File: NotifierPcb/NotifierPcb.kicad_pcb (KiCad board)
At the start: 2 copper layers, 81.6 x 97.9 mm, 30 parts, among them IC1 CD4067BEE4, IC2 ESP32-WROOM-32E__8MB_, J1 RC_433_MHZ_RF, J2 UART_Conn, J3 Power_Conn, J5 Vcc, J6 Vcc, U1 HT75xx-1-SOT89

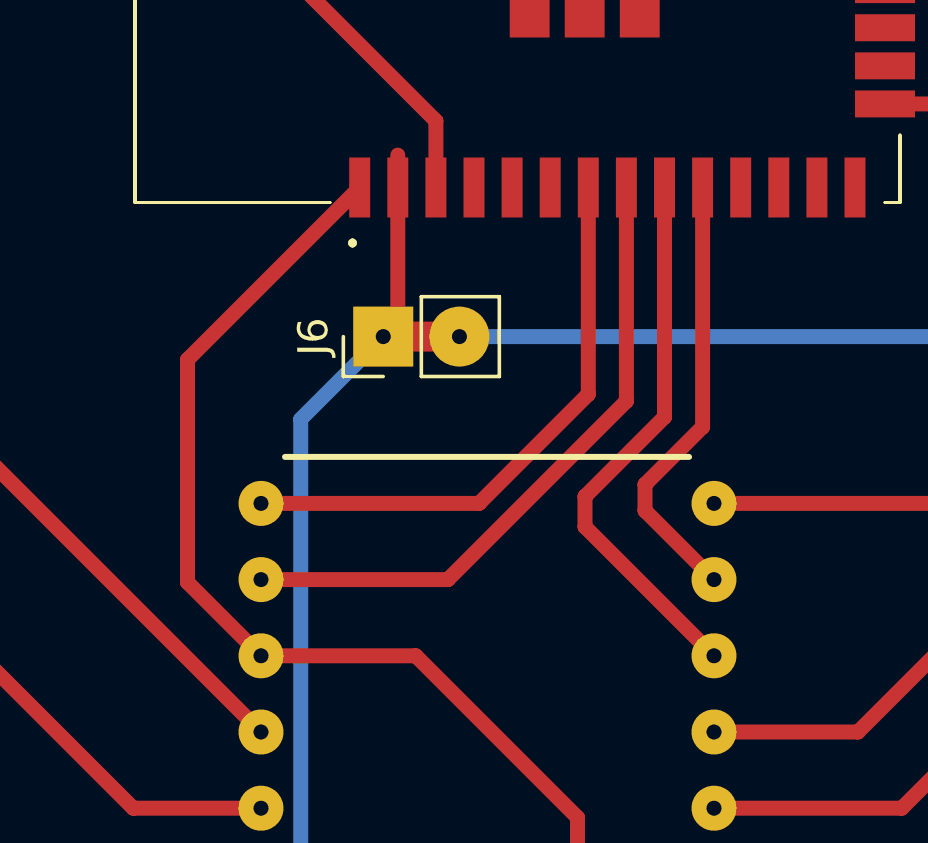
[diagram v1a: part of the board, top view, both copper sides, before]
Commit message: FIX: using only-input pin
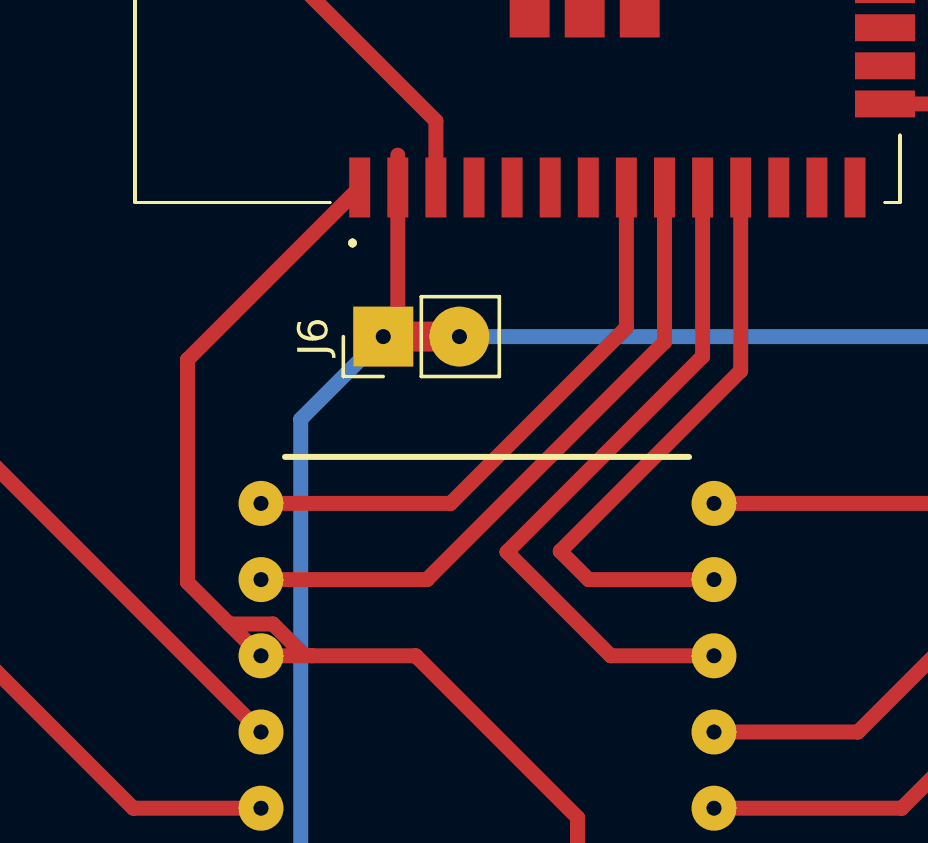
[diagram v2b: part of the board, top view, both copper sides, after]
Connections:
- IC2 pad 10: BIT1 -> BIT0
- IC2 pad 11: unconnected-(IC2-Pad11) -> BIT1
- IC2 pad 7: BIT3 -> unconnected-(IC2-Pad7)
- IC2 pad 8: BIT2 -> BIT3
- IC2 pad 9: BIT0 -> BIT2
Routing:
- net BIT1: track 14.8 -> 20.1 mm
- net BIT0: track 18.5 -> 23.2 mm
- net GND: track 197.6 -> 200.5 mm
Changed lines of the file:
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@@
   (net 25 "unconnected-(IC2-Pad5)")
   (net 26 "unconnected-(IC2-Pad6)")
-  (net 27 "unconnected-(IC2-Pad11)")
+  (net 27 "unconnected-(IC2-Pad7)")
   (net 28 "unconnected-(IC2-Pad12)")
   (net 29 "unconnected-(IC2-Pad13)")
@@
       (net 26 "unconnected-(IC2-Pad6)") (pinfunction "IO34") (pintype "passive"))
     (pad "7" smd rect (at -8.5 2.36 180) (size 0.7 2) (layers "F.Cu" "F.Paste" "F.Mask")
-      (net 13 "BIT3") (pinfunction "IO35") (pintype "passive"))
+      (net 27 "unconnected-(IC2-Pad7)") (pinfunction "IO35") (pintype "passive"))
     (pad "8" smd rect (at -8.5 3.63 180) (size 0.7 2) (layers "F.Cu" "F.Paste" "F.Mask")
-      (net 14 "BIT2") (pinfunction "IO32") (pintype "passive"))
+      (net 13 "BIT3") (pinfunction "IO32") (pintype "passive"))
     (pad "9" smd rect (at -8.5 4.9 180) (size 0.7 2) (layers "F.Cu" "F.Paste" "F.Mask")
-      (net 10 "BIT0") (pinfunction "IO33") (pintype "passive"))
+      (net 14 "BIT2") (pinfunction "IO33") (pintype "passive"))
     (pad "10" smd rect (at -8.5 6.17 180) (size 0.7 2) (layers "F.Cu" "F.Paste" "F.Mask")
-      (net 11 "BIT1") (pinfunction "IO25") (pintype "passive"))
+      (net 10 "BIT0") (pinfunction "IO25") (pintype "passive"))
     (pad "11" smd rect (at -8.5 7.44 180) (size 0.7 2) (layers "F.Cu" "F.Paste" "F.Mask")
-      (net 27 "unconnected-(IC2-Pad11)") (pinfunction "IO26") (pintype "passive"))
+      (net 11 "BIT1") (pinfunction "IO26") (pintype "passive"))
     (pad "12" smd rect (at -8.5 8.71 180) (size 0.7 2) (layers "F.Cu" "F.Paste" "F.Mask")
       (net 28 "unconnected-(IC2-Pad12)") (pinfunction "IO27") (pintype "passive"))
@@
   (segment (start 168.85 74.15) (end 168.9 74.15) (width 1) (layer "F.Cu") (net 9))
   (segment (start 147.55 90.65) (end 152.35 90.65) (width 0.5) (layer "F.Cu") (net 9))
-  (segment (start 145.9 80.15) (end 143.25 82.8) (width 0.5) (layer "F.Cu") (net 10))
-  (segment (start 145.9 72.5) (end 145.9 80.15) (width 0.5) (layer "F.Cu") (net 10))
-  (segment (start 143.25 83.81) (end 147.55 88.11) (width 0.5) (layer "F.Cu") (net 10))
-  (segment (start 143.25 82.8) (end 143.25 83.81) (width 0.5) (layer "F.Cu") (net 10))
-  (segment (start 147.17 80.48) (end 145.25 82.4) (width 0.5) (layer "F.Cu") (net 11))
-  (segment (start 147.17 72.5) (end 147.17 80.48) (width 0.5) (layer "F.Cu") (net 11))
-  (segment (start 145.25 83.27) (end 147.55 85.57) (width 0.5) (layer "F.Cu") (net 11))
-  (segment (start 145.25 82.4) (end 145.25 83.27) (width 0.5) (layer "F.Cu") (net 11))
+  (segment (start 140.65 84.65) (end 144.11 88.11) (width 0.5) (layer "F.Cu") (net 10))
+  (segment (start 147.17 78.13) (end 140.65 84.65) (width 0.5) (layer "F.Cu") (net 10))
+  (segment (start 147.17 72.5) (end 147.17 78.13) (width 0.5) (layer "F.Cu") (net 10))
+  (segment (start 144.11 88.11) (end 147.55 88.11) (width 0.5) (layer "F.Cu") (net 10))
+  (segment (start 148.44 72.5) (end 148.44 78.61) (width 0.5) (layer "F.Cu") (net 11))
+  (segment (start 148.44 78.61) (end 142.425 84.625) (width 0.5) (layer "F.Cu") (net 11))
+  (segment (start 143.37 85.57) (end 147.55 85.57) (width 0.5) (layer "F.Cu") (net 11))
+  (segment (start 142.425 84.625) (end 143.37 85.57) (width 0.5) (layer "F.Cu") (net 11))
   (segment (start 111.55 58.672349) (end 111.55 63.535) (width 0.5) (layer "F.Cu") (net 12))
   (segment (start 144.75 118.6) (end 144.75 122.05) (width 0.5) (layer "F.Cu") (net 12))
@@
   (segment (start 143.0665 116.9165) (end 144.75 118.6) (width 0.5) (layer "F.Cu") (net 12))
   (segment (start 155.72 83.03) (end 147.55 83.03) (width 0.5) (layer "F.Cu") (net 12))
-  (segment (start 132.45 88.11) (end 137.61 88.11) (width 0.5) (layer "F.Cu") (net 12))
   (segment (start 156.115 69.715) (end 158.05 71.65) (width 0.5) (layer "F.Cu") (net 12))
   (segment (start 103.775 57.275) (end 110.152651 57.275) (width 0.5) (layer "F.Cu") (net 12))
@@
   (segment (start 128.46 48.22) (end 135.74 55.5) (width 0.5) (layer "F.Cu") (net 12))
   (segment (start 118.007651 58.672349) (end 128.46 48.22) (width 0.5) (layer "F.Cu") (net 12))
+  (segment (start 130 85.66) (end 131.17 86.83) (width 0.5) (layer "F.Cu") (net 12))
   (segment (start 177 67.5) (end 174.75 69.75) (width 0.5) (layer "F.Cu") (net 12))
   (segment (start 167.81 67.71) (end 167.81 61.3) (width 0.5) (layer "F.Cu") (net 12))
   (segment (start 110.152651 57.275) (end 111.55 58.672349) (width 0.5) (layer "F.Cu") (net 12))
   (segment (start 173.9 49.35) (end 173.9 52.35) (width 0.5) (layer "F.Cu") (net 12))
+  (segment (start 132.45 88.11) (end 134.14 88.11) (width 0.5) (layer "F.Cu") (net 12))
   (segment (start 130 78.24) (end 130 85.66) (width 0.5) (layer "F.Cu") (net 12))
   (segment (start 174.75 69.75) (end 169.85 69.75) (width 0.5) (layer "F.Cu") (net 12))
@@
   (segment (start 143.0665 123.7335) (end 142.85 123.95) (width 1) (layer "F.Cu") (net 12))
   (segment (start 153.25 69.715) (end 156.115 69.715) (width 0.5) (layer "F.Cu") (net 12))
+  (segment (start 134.14 88.11) (end 137.61 88.11) (width 0.5) (layer "F.Cu") (net 12))
+  (segment (start 132.85 87.05) (end 133.91 88.11) (width 0.5) (layer "F.Cu") (net 12))
+  (segment (start 131.17 86.83) (end 132.45 88.11) (width 0.5) (layer "F.Cu") (net 12))
   (segment (start 137.61 88.11) (end 143 93.5) (width 0.5) (layer "F.Cu") (net 12))
   (segment (start 111.55 58.672349) (end 118.007651 58.672349) (width 0.5) (layer "F.Cu") (net 12))
@@
   (segment (start 143 93.5) (end 143 116.85) (width 0.5) (layer "F.Cu") (net 12))
   (segment (start 169.85 69.75) (end 167.81 67.71) (width 0.5) (layer "F.Cu") (net 12))
-  (segment (start 130 85.66) (end 132.45 88.11) (width 0.5) (layer "F.Cu") (net 12))
-  (segment (start 139.72 83.03) (end 132.45 83.03) (width 0.5) (layer "F.Cu") (net 13))
-  (segment (start 143.36 72.5) (end 143.36 79.39) (width 0.5) (layer "F.Cu") (net 13))
-  (segment (start 143.36 79.39) (end 139.72 83.03) (width 0.5) (layer "F.Cu") (net 13))
-  (segment (start 138.68 85.57) (end 132.45 85.57) (width 0.5) (layer "F.Cu") (net 14))
-  (segment (start 144.63 79.62) (end 138.68 85.57) (width 0.5) (layer "F.Cu") (net 14))
-  (segment (start 144.63 72.5) (end 144.63 79.62) (width 0.5) (layer "F.Cu") (net 14))
+  (segment (start 131.39 87.05) (end 132.85 87.05) (width 0.5) (layer "F.Cu") (net 12))
+  (segment (start 132.45 83.03) (end 138.77 83.03) (width 0.5) (layer "F.Cu") (net 13))
+  (segment (start 144.63 77.17) (end 144.63 72.5) (width 0.5) (layer "F.Cu") (net 13))
+  (segment (start 138.77 83.03) (end 144.63 77.17) (width 0.5) (layer "F.Cu") (net 13))
+  (segment (start 145.9 77.65) (end 145.9 72.5) (width 0.5) (layer "F.Cu") (net 14))
+  (segment (start 137.98 85.57) (end 145.9 77.65) (width 0.5) (layer "F.Cu") (net 14))
+  (segment (start 132.45 85.57) (end 137.98 85.57) (width 0.5) (layer "F.Cu") (net 14))
   (segment (start 114.65 73.1) (end 114.9 73.1) (width 1) (layer "F.Cu") (net 15))
   (segment (start 114.9 73.1) (end 132.45 90.65) (width 0.5) (layer "F.Cu") (net 15))

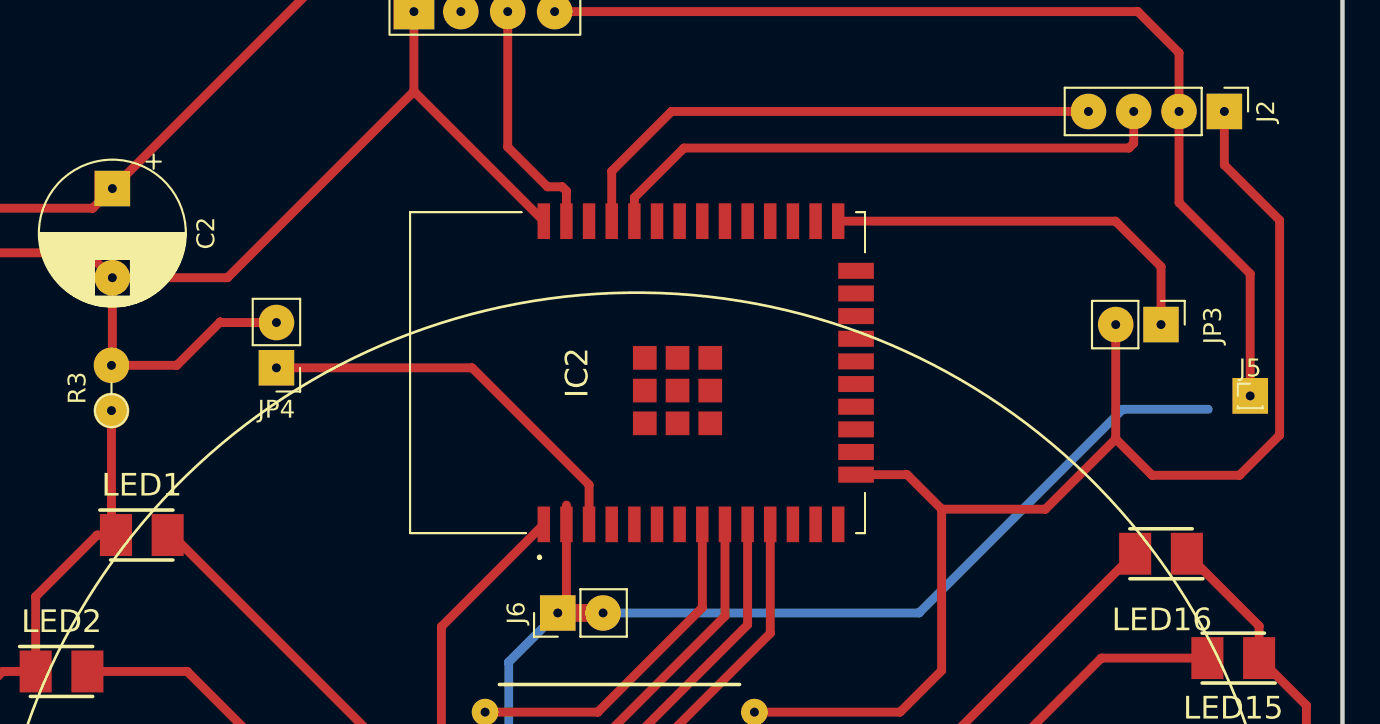
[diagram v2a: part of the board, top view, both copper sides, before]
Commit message: add pullup resistor for strapping pins
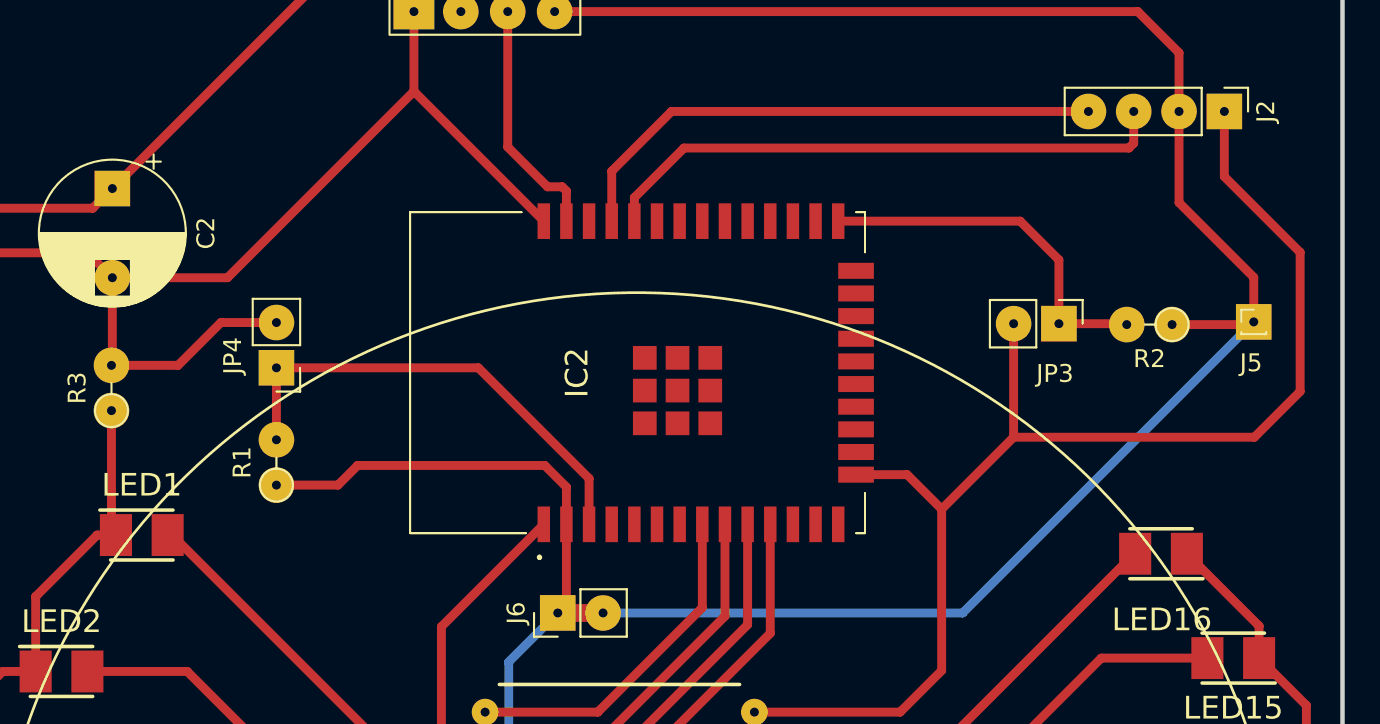
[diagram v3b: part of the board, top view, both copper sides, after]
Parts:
- added R1: 10kΩ, Resistor_THT:R_Axial_DIN0204_L3.6mm_D1.6mm_P2.54mm_Vertical, F.Cu at (120.8, 70.3)
- added R2: 10kΩ, Resistor_THT:R_Axial_DIN0204_L3.6mm_D1.6mm_P2.54mm_Vertical, F.Cu at (171.0, 61.3)
- JP3: value Boot_Jumper_Download -> Boot_Jumper
- JP4: value Enable_Jumper -> En_Jump
- moved JP3 5.73 mm to (164.6, 61.2)
- moved J5 4.15 mm to (175.6, 61.1)
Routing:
- net +3.3V: track 240.3 -> 263.7 mm
- net ESP32_EN: track 22.5 -> 26.7 mm
- net BOOT: track 22.4 -> 20.7 mm
- net GND: track 200.5 -> 198.9 mm

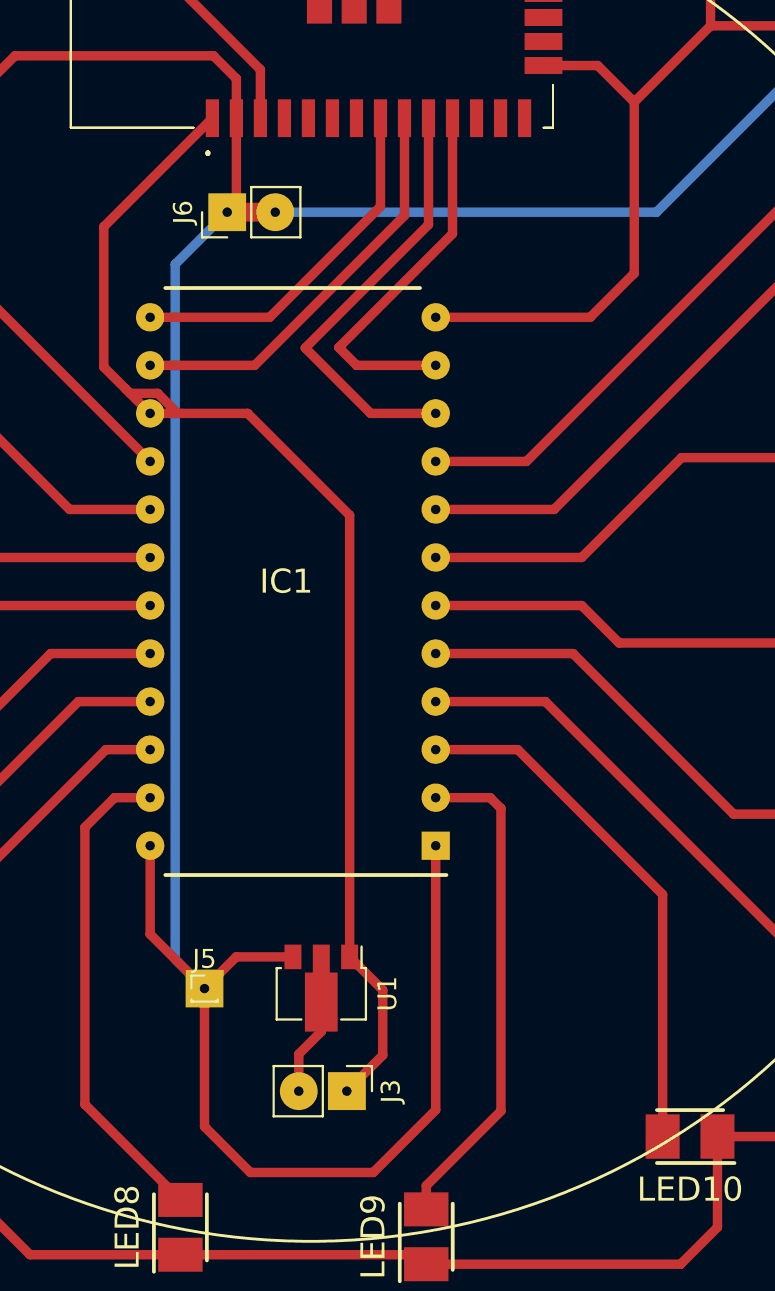
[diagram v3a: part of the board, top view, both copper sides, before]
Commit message: control demux input
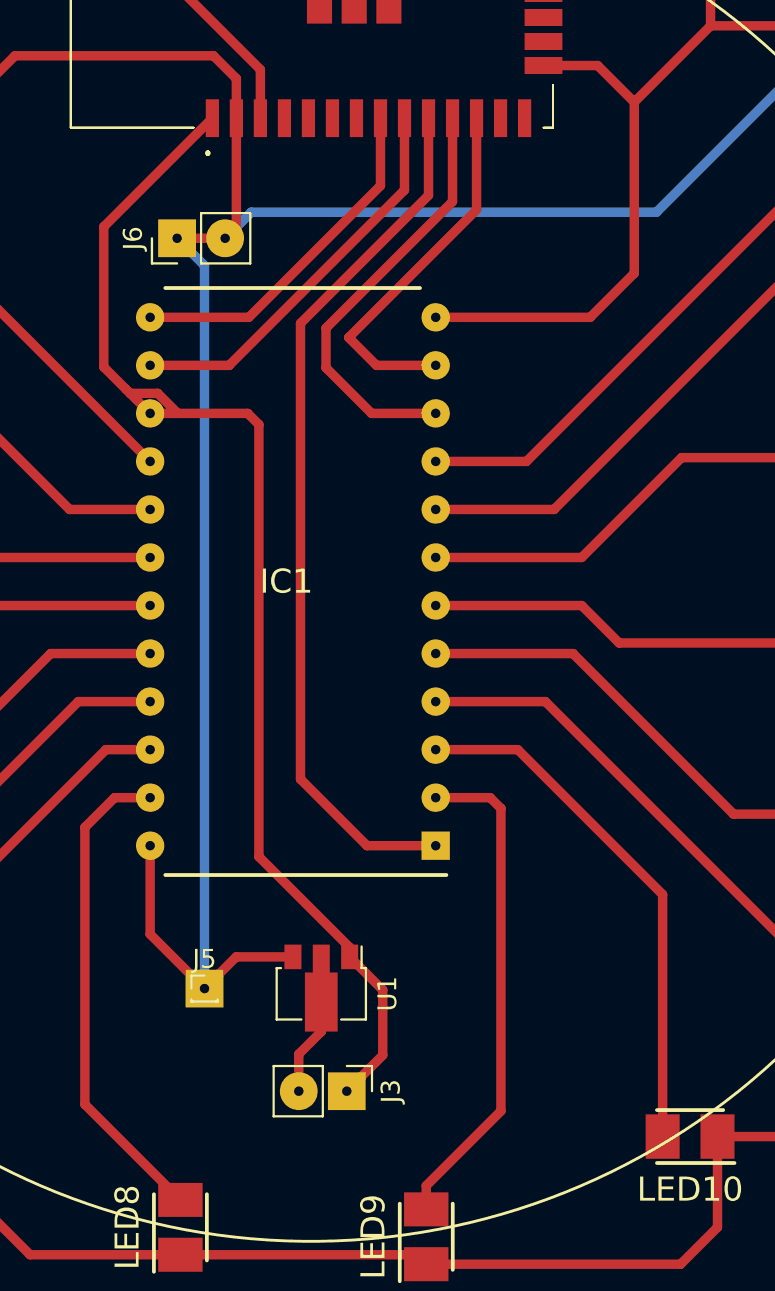
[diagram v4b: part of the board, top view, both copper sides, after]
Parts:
- JP3: value Boot_Jumper -> Boot_Jumper_Download
- JP4: value En_Jump -> Enable_Jumper
- moved J6 2.99 mm to (133.9, 78.8)
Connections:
- IC1 pad 1: +3.3V -> DEMUX_IN
- IC2 pad 10: BIT0 -> DEMUX_IN
- IC2 pad 11: BIT1 -> BIT0
- IC2 pad 12: unconnected-(IC2-Pad12) -> BIT1
- R1 pad 1: +3.3V -> VCC
- R1 pad e: ESP32_EN -> (no net)
- R2 pad 1: +3.3V -> VCC
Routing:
- net DEMUX_IN: track 0.00 -> 46.4 mm
- net +3.3V: track 263.7 -> 229.9 mm
- net BIT2: track 21.9 -> 21.1 mm
- net BIT3: track 19.3 -> 18.6 mm
- net BIT1: track 20.1 -> 19.6 mm
